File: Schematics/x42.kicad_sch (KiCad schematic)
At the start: 70 parts, among them J31 CAN IN, J32 EXTRUDER HEATER, J33 FAN1, J34 FAN2, J36 EXTRUDER THERMISTOR, J37 STOP-1, J38 STOP-2, J39 STOP-3, J40 BLTOUCH, J41 I2C, J42 NEOPIXEL, Q7 NMOS, Q8 FAN1, Q9 FAN2, SW4 X42 RESET, SW5 X42 BOOT, U20 STM32G0B1CBTx, U21 TJA1051T-3, U22 74LVC1G17, U23 TPS54302, U24 AMS1117CD-3.3, U25 74LVC1G17, U26 ADXL345BCCZ, Y3 8MHZ

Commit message: Update Schematics
Update CM4, X42, XYmatics-E64 schematics
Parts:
- removed J32: EXTRUDER HEATER, symbol Connector_Generic:Conn_01x02
- added C74: 22NF, symbol Device:C
- added C75: 4.7UF, symbol Device:C
- added C76, C77, C78, C79, C80, C82, C83: 100NF, symbol Device:C
- added C81: 100UF, symbol Device:C_Polarized
- added C84: 10UF, symbol Device:C
- added D14, D15: B340, Diode_SMD:D_SMC, symbol Diode:B340
- added D16: X42 STATUS, symbol Device:LED
- added D17: X42 POWER, symbol Device:LED
- added J26: X42 HOTEND, symbol Connector_Generic:Conn_01x02
- added J43: SPINDLE/LASER, symbol Connector_Generic:Conn_01x02
- added J44: EXTRUDER, symbol Connector_Generic:Conn_01x04
- added J45: X42 SWD, symbol Connector:Conn_01x04_Pin
- added L4: 120R, symbol Device:L_Ferrite
- added Q10: X42 MOSFET, symbol Simulation_SPICE:NMOS
- added R68, R75, R78, R79: 10K, symbol Device:R
- added R69: 20K, symbol Device:R
- added R70: 20, symbol Device:R
- added R73, R74: 0, symbol Device:R
- added R76: 200, symbol Device:R
- added R77: 1.5K, symbol Device:R
- added U27: 74LVC1G17, symbol 74xGxx:74LVC1G17
- added U29: TMC2209-LA-T, TMC2209-LA-T:QFN50P500X500X90-29N, symbol TMC2209-LA-T:TMC2209-LA-T
- C59: value 0.1UF -> 100NF
- J36: value EXTRUDER THERMISTOR -> X42 THERMISTOR
- Q7: value NMOS -> E0-HEAT
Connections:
- net 24V: now also C76.1, C78.2, C79.2, C80.2, C81.1, D14.1 (K), D15.1 (K), J26.1 (Pin_1), J43.1 (Pin_1), U29.22 (VS), U29.28 (VS)
- net 3V3: now also C77.2, R75.1, U29.15 (VCC_IO)
- net 5V: now also U27.5 (VCC)
- net E0-HE: now also U20.14 (PA3); no longer U20.13 (PA2)
- net E0-TH: now also U20.13 (PA2); no longer U20.14 (PA3)
- net GND: now also U20.30 (PC6), C75.1, C77.1, C82.2, C83.2, C84.2, D16.1 (K), D17.1 (K), J45.1 (Pin_1), Q10.3 (S), R68.2, R69.1, R73.2, R74.2, R78.1, U27.2, U27.3 (GND), U29.13 (CLK), U29.18 (GND), U29.20 (STDBY), U29.29 (EXP), U29.3 (GND), U29.7 (SPREAD)
- net X42-3V3: now also C82.1, C83.1, C84.1, L4.1, L4.2, R77.1
- net at Q7.1 (D): now also D15.2 (A), J26.2 (Pin_2)
- net X42-FET: now reaches U20.15 (PA4)
- net X42-FET: now also R68.1
- net at U20.3 (PC15): now also R76.1
- net X42-SWCLK: now reaches U20.34 (PA10/PA12)
- net X42-SWCLK: now also J45.2 (Pin_2), R78.2
- net X42-SWDIO: now reaches U20.35 (PA13)
- net X42-SWDIO: now also J45.3 (Pin_3), R79.2
- net E0-STEP: now reaches U20.38 (PD0)
- net E0-STEP: now also U29.16 (STEP)
- net E0-DIR: now reaches U20.39 (PD1)
- net E0-DIR: now also U29.19 (DIR)
- net E0-EN: now reaches U20.40 (PD2)
- net E0-EN: now also R75.2, U29.2 (~{EN})
- net E0-UART: now reaches U20.41 (PD3)
- net E0-UART: now also U29.14 (~{PD}_UART)
- new net: D17.2 (A), R77.2
- new net: D16.2 (A), R76.2
- new net: R69.2, R70.1, U27.4
- new net: D14.2 (A), J43.2 (Pin_2), Q10.1 (D)
- new net: Q10.2 (G), R70.2
- new net: C78.1, C79.1, C80.1, C81.2
- new net: R74.1, U29.27 (BRB)
- new net: J44.4 (Pin_4), U29.1 (OB2)
- new net: J44.1 (Pin_1), U29.21 (OA2)
- new net: R73.1, U29.23 (BRA)
- new net: J44.2 (Pin_2), U29.24 (OA1)
- new net: J44.3 (Pin_3), U29.26 (OB1)
- new net: C74.1, U29.4 (CPO)
- new net: C74.2, U29.5 (CPI)
- new net: C76.2, U29.6 (VCP)
- new net: C75.2, U29.8 (5VOUT)
- new net +3V3: J45.4 (Pin_4), R79.1
- no-connect marks 3 -> 24
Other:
- company: (none) -> XYmatics E64
- title: (none) -> X42
- moved on the sheet: C56, C59, C61, C62, C63, C64, C65, C66, C67, C68, C69, C70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

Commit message: Update X42 schematics, Add project PCB
Removed Neopixel and BLTouch breakouts from X42, added X42 PCB (unfinished)
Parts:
- removed C71: 15PF, symbol Device:C
- removed C80: 100NF, symbol Device:C
- removed C81: 100UF, symbol Device:C_Polarized
- removed D10, D11, D15: B340, Diode_SMD:D_SMC, symbol Diode:B340
- removed J38: STOP-2, Connector_JST:JST_XH_B3B-XH-A_1x03_P2.50mm_Vertical, symbol Connector_Generic:Conn_01x03
- removed J39: STOP-3, Connector_JST:JST_XH_B3B-XH-A_1x03_P2.50mm_Vertical, symbol Connector_Generic:Conn_01x03
- removed J40: BLTOUCH, Connector_JST:JST_XH_B5B-XH-A_1x05_P2.50mm_Vertical, symbol Connector_Generic:Conn_01x05
- removed J42: NEOPIXEL, symbol Connector_Generic:Conn_01x03
- removed Q7: E0-HEAT, symbol Simulation_SPICE:NMOS
- removed R59, R60: 10K, symbol Device:R
- removed R61: 4.7K, symbol Device:R
- removed R62: 100, symbol Device:R
- removed U25: 74LVC1G17, symbol 74xGxx:74LVC1G17
- added C80: 100UF, Capacitor_SMD:CP_Elec_5x3, symbol Device:C_Polarized
- added D10, D11: 1N5819WS, Diode_SMD:D_SOD-323, symbol Diode:1N5819WS
- added H1, H2: MountingHole_Pad, MountingHole:MountingHole_3mm_Pad, symbol Mechanical:MountingHole_Pad
- added Q7: E0-HEAT, Package_TO_SOT_SMD:Vishay_PowerPAK_SC70-6L_Single, symbol Transistor_FET:SiA462DJ
- C56, C57, C58, C59, C61, C63, C64, C65, C66, C69, C72, C73, C74, C75, C76, C77, C78, C79, C82, C83, C84: footprint (none) -> Capacitor_SMD:C_0805_2012Metric
- C62, C67, C68, C70: footprint (none) -> Capacitor_SMD:CP_Elec_5x3
- D16: value X42 STATUS -> STATUS; footprint (none) -> LED_SMD:LED_0805_2012Metric
- D17: footprint (none) -> LED_SMD:LED_0805_2012Metric
- J26: value X42 HOTEND -> HOTEND; footprint (none) -> Connector_JST:JST_XH_B2B-XH-A_1x02_P2.50mm_Vertical
- J31: footprint (none) -> Connector_Molex:Molex_Micro-Fit_3.0_43045-0400_2x02_P3.00mm_Horizontal
- J33, J34: footprint Connector_JST:JST_XH_B2B-XH-A_1x02_P2.50mm_Vertical -> Connector_PinHeader_2.54mm:PinHeader_1x02_P2.54mm_Vertical_SMD_Pin1Right
- J36: value X42 THERMISTOR -> TEMP; footprint (none) -> Connector_JST:JST_XH_B2B-XH-A_1x02_P2.50mm_Vertical
- J37: value STOP-1 -> STOP
- J41, J44: footprint (none) -> Connector_JST:JST_XH_B4B-XH-A_1x04_P2.50mm_Vertical
- J43: footprint (none) -> Connector_JST:JST_XH_B2B-XH-A_1x02_P2.50mm_Vertical
- J45: value X42 SWD -> SWD; footprint (none) -> Connector_PinHeader_2.54mm:PinHeader_1x04_P2.54mm_Vertical_SMD_Pin1Right
- L3: footprint (none) -> Inductor_SMD:L_6.3x6.3_H3
- L4: footprint (none) -> Inductor_SMD:L_0805_2012Metric
- Q10: footprint (none) -> Package_TO_SOT_SMD:TO-252-2
- Q8, Q9: footprint (none) -> Package_TO_SOT_SMD:SOT-23
- R40, R41, R42, R43, R44, R45, R46, R47, R51, R54, R55, R56, R57, R58, R63, R64, R65, R66, R67, R68, R69, R70, R73, R74, R75, R76, R77, R78, R79: footprint (none) -> Resistor_SMD:R_0805_2012Metric
- R52, R53: value 2.37 -> 2.37K; footprint (none) -> Resistor_SMD:R_0805_2012Metric
- SW4: value X42 RESET -> EN; footprint (none) -> Button_Switch_SMD:SW_Tactile_SPST_NO_Straight_CK_PTS636Sx25SMTRLFS
- SW5: value X42 BOOT -> BOOT; footprint (none) -> Button_Switch_SMD:SW_Tactile_SPST_NO_Straight_CK_PTS636Sx25SMTRLFS
- U22, U27: footprint (none) -> Package_TO_SOT_SMD:SOT-23-5
- U24: footprint Package_TO_SOT_SMD:TO-252-3_TabPin2 -> Package_TO_SOT_SMD:TO-252-2
- U26: footprint ADXL345BCCZ:IC_ADXL345BCCZ -> ADXL345:IC_ADXL345BCCZ
- U29: footprint TMC2209-LA-T:QFN50P500X500X90-29N -> TMC2209-LA:QFN50P500X500X90-29N
- Y3: footprint (none) -> Crystal:Crystal_SMD_Abracon_ABM3B-4Pin_5.0x3.2mm
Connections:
- net +3V3 is gone; now on net 3V3: J45.4 (Pin_4), R79.1
- net 24V: now also C80.1, D10.1 (K), D11.1 (K)
- net GND: now also C78.1, C79.1, U29.10 (MS2_AD1), U29.9 (MS1_AD0), C80.2, H1.1, H2.1, Q7.4 (S); no longer U20.30 (PC6)
- net at J34.2 (Pin_2), Q9.1 (D): now also D11.2 (A)
- net CAN-: now reaches J31.4 (Pin_4), R41.1, U21.6 (CANL)
- net CAN+: now reaches J31.3 (Pin_3), R40.2, U21.7 (CANH)
- net at R45.2: now also Q7.3 (G)
- net at J26.2 (Pin_2): now also Q7.1 (D)
- net at J33.2 (Pin_2), Q8.1 (D): now also D10.2 (A)
- net ENDSTOP-1 renamed X42-ENDSTOP
- net ENDSTOP-2: no longer names the net of U20.45 (PB6)
- net ENDSTOP-3: no longer names the net of U20.46 (PB7)
- no-connect marks 24 -> 27
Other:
- moved on the sheet: J33, J34, Q8, Q9, R46, R47

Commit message: Update X42 schematics, Update X42 PCB
Removed X42 Endstops (re-add in next revision)
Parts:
- removed J37: STOP, Connector_JST:JST_XH_B3B-XH-A_1x03_P2.50mm_Vertical, symbol Connector_Generic:Conn_01x03
- removed R58: 10K, Resistor_SMD:R_0805_2012Metric, symbol Device:R
- J41: footprint Connector_JST:JST_XH_B4B-XH-A_1x04_P2.50mm_Vertical -> Connector_PinHeader_2.54mm:PinHeader_1x04_P2.54mm_Vertical_SMD_Pin1Right
- J43: footprint Connector_JST:JST_XH_B2B-XH-A_1x02_P2.50mm_Vertical -> Connector_PinHeader_2.54mm:PinHeader_1x02_P2.54mm_Vertical_SMD_Pin1Right
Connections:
- net 3V3: now also L4.1
- net X42-3V3: no longer L4.1
- net X42-SCL: now also U20.42 (PB3)
- net X42-SDA: now also U20.43 (PB4)
- net GND renamed XGND
- net X42-ENDSTOP: no longer names the net of U20.44 (PB5)
- no-connect marks 27 -> 26
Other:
- moved on the sheet: D11, J34, Q9, R47

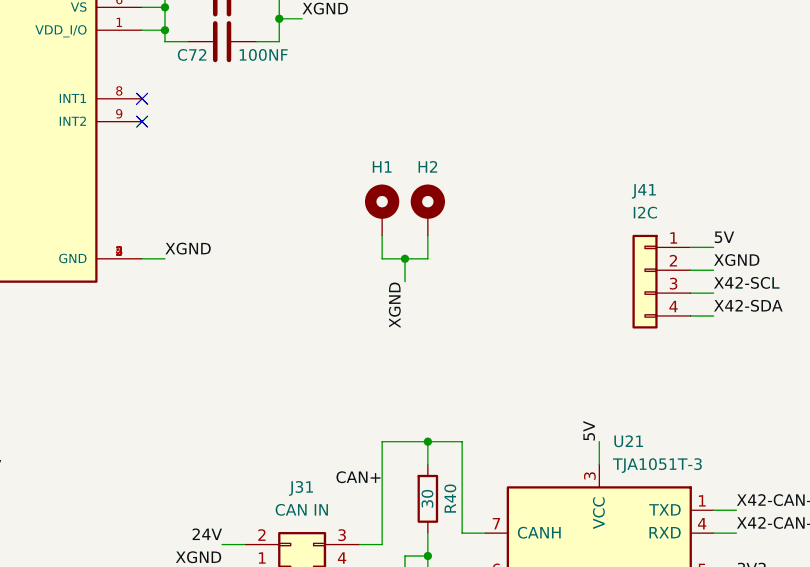
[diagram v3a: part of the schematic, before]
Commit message: Update E64 schematics
Finish E64 PCB
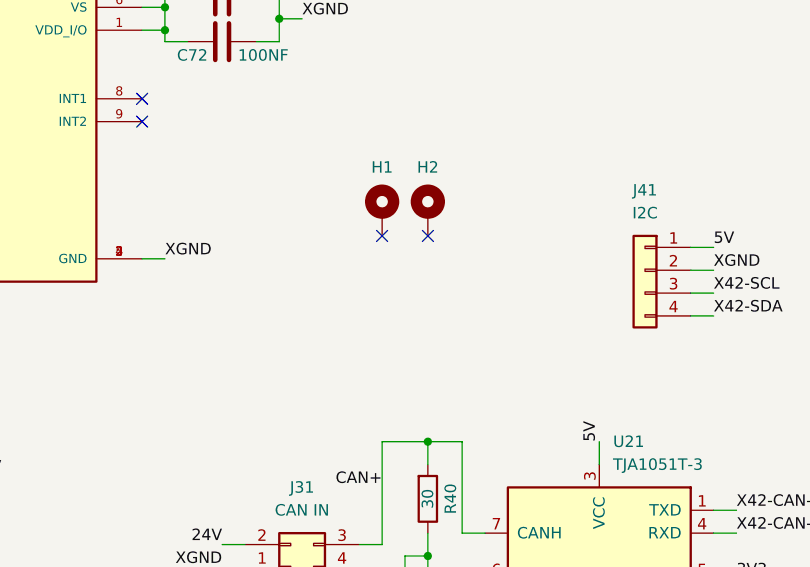
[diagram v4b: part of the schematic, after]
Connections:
- net XGND: no longer H1.1, H2.1
- no-connect marks 26 -> 28
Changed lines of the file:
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@@
 	)
 	(junction
-		(at 332.74 55.88)
-		(diameter 0)
-		(color 0 0 0 0)
-	)
-	(junction
 		(at 285.75 139.7)
 		(diameter 0)
@@
 	)
 	(no_connect
+		(at 330.2 53.34)
+	)
+	(no_connect
 		(at 116.84 73.66)
 	)
@@
 	)
 	(no_connect
+		(at 335.28 53.34)
+	)
+	(no_connect
 		(at 60.96 78.74)
 	)
@@
 	(wire
 		(pts
-			(xy 330.2 53.34) (xy 330.2 55.88)
-		)
-		(stroke
-			(width 0)
-			(type default)
-		)
-	)
-	(wire
-		(pts
 			(xy 152.4 168.91) (xy 160.02 168.91)
 		)
@@
 	(wire
 		(pts
-			(xy 330.2 55.88) (xy 332.74 55.88)
-		)
-		(stroke
-			(width 0)
-			(type default)
-		)
-	)
-	(wire
-		(pts
 			(xy 330.2 149.86) (xy 330.2 152.4)
 		)
@@
 	(wire
 		(pts
-			(xy 332.74 55.88) (xy 332.74 58.42)
-		)
-		(stroke
-			(width 0)
-			(type default)
-		)
-	)
-	(wire
-		(pts
 			(xy 204.47 20.32) (xy 207.01 20.32)
 		)
@@
 	(wire
 		(pts
-			(xy 335.28 53.34) (xy 335.28 55.88)
-		)
-		(stroke
-			(width 0)
-			(type default)
-		)
-	)
-	(wire
-		(pts
 			(xy 370.84 139.7) (xy 368.3 139.7)
 		)
@@
 	(wire
 		(pts
-			(xy 332.74 55.88) (xy 335.28 55.88)
-		)
-		(stroke
-			(width 0)
-			(type default)
-		)
-	)
-	(wire
-		(pts
 			(xy 46.99 139.7) (xy 46.99 142.24)
 		)
@@
 		(effects
 			(font
-				(size 1.27 1.27)
-			)
-			(justify right bottom)
-		)
-	)
-	(label "XGND"
-		(at 332.74 58.42 270)
-		(effects
-			(font
